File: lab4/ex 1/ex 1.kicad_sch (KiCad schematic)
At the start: 6 parts, among them J1 Conn_01x02_Male, SW1 SW_SPDT

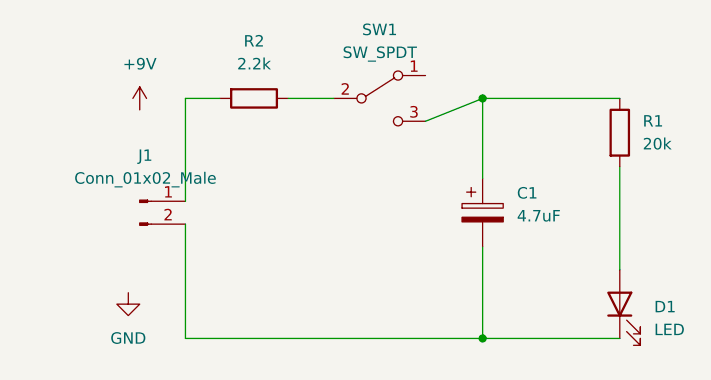
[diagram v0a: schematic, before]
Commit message: Updated schematics to include footprints and created a pcb layout
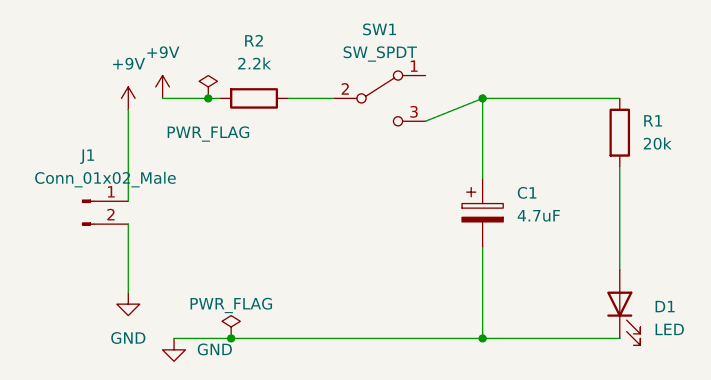
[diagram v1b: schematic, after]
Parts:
- C1: footprint (none) -> Capacitor_THT:C_Radial_D5.0mm_H5.0mm_P2.00mm
- D1: footprint (none) -> LED_THT:LED_D5.0mm
- J1: footprint (none) -> Connector_JST:JST_PH_B2B-PH-K_1x02_P2.00mm_Vertical
- R1, R2: footprint (none) -> Resistor_THT:R_Axial_DIN0516_L15.5mm_D5.0mm_P20.32mm_Horizontal
- SW1: footprint (none) -> Button_Switch_THT:SW_E-Switch_EG1224_SPDT_Angled
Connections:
- net +9V: now also J1.1 (Pin_1), R2.2
- net GND: now also C1.2, D1.1 (K), J1.2 (Pin_2)
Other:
- moved on the sheet: J1
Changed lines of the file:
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@@
 (kicad_sch (version 20211123) (generator eeschema)
   (paper "A4")
+  (junction (at 110.49 69.85) (diameter 0) (color 0 0 0 0)
+  )
   (junction (at 140.97 69.85) (diameter 0) (color 0 0 0 0)
   )
   (junction (at 140.97 96.52) (diameter 0) (color 0 0 0 0)
   )
+  (junction (at 113.03 96.52) (diameter 0) (color 0 0 0 0)
+  )
   (wire (pts (xy 140.97 96.52) (xy 156.21 96.52))
     (stroke (width 0) (type default) (color 0 0 0 0))
@@
     (stroke (width 0) (type default) (color 0 0 0 0))
   )
-  (wire (pts (xy 107.95 96.52) (xy 140.97 96.52))
-    (stroke (width 0) (type default) (color 0 0 0 0))
-  )
-  (wire (pts (xy 107.95 83.82) (xy 107.95 96.52))
-    (stroke (width 0) (type default) (color 0 0 0 0))
-  )
-  (wire (pts (xy 107.95 81.28) (xy 107.95 69.85))
+  (wire (pts (xy 106.68 96.52) (xy 113.03 96.52))
     (stroke (width 0) (type default) (color 0 0 0 0))
   )
@@
     (stroke (width 0) (type default) (color 0 0 0 0))
   )
+  (wire (pts (xy 110.49 69.85) (xy 111.76 69.85))
+    (stroke (width 0) (type default) (color 0 0 0 0))
+  )
+  (wire (pts (xy 101.6 71.12) (xy 101.6 81.28))
+    (stroke (width 0) (type default) (color 0 0 0 0))
+  )
+  (wire (pts (xy 113.03 96.52) (xy 140.97 96.52))
+    (stroke (width 0) (type default) (color 0 0 0 0))
+  )
   (wire (pts (xy 156.21 77.47) (xy 156.21 88.9))
     (stroke (width 0) (type default) (color 0 0 0 0))
   )
+  (wire (pts (xy 101.6 91.44) (xy 101.6 83.82))
+    (stroke (width 0) (type default) (color 0 0 0 0))
+  )
   (wire (pts (xy 140.97 86.36) (xy 140.97 96.52))
     (stroke (width 0) (type default) (color 0 0 0 0))
   )
-  (wire (pts (xy 107.95 69.85) (xy 111.76 69.85))
-    (stroke (width 0) (type default) (color 0 0 0 0))
-  )
-  (symbol (lib_id "power:+9V") (at 102.87 71.12 0) (unit 1)
-    (in_bom yes) (on_board yes)
-    (property "Reference" "#PWR01" (id 0) (at 102.87 74.93 0)
-      (effects (font (size 1.27 1.27)) hide)
-    )
-    (property "Value" "+9V" (id 1) (at 102.87 66.04 0))
-    (property "Footprint" "" (id 2) (at 102.87 71.12 0)
-      (effects (font (size 1.27 1.27)) hide)
-    )
-    (property "Datasheet" "" (id 3) (at 102.87 71.12 0)
+  (wire (pts (xy 105.41 69.85) (xy 110.49 69.85))
+    (stroke (width 0) (type default) (color 0 0 0 0))
+  )
+  (symbol (lib_id "power:+9V") (at 101.6 71.12 0) (unit 1)
+    (in_bom yes) (on_board yes)
+    (property "Reference" "#PWR01" (id 0) (at 101.6 74.93 0)
+      (effects (font (size 1.27 1.27)) hide)
+    )
+    (property "Value" "+9V" (id 1) (at 101.6 66.04 0))
+    (property "Footprint" "" (id 2) (at 101.6 71.12 0)
+      (effects (font (size 1.27 1.27)) hide)
+    )
+    (property "Datasheet" "" (id 3) (at 101.6 71.12 0)
       (effects (font (size 1.27 1.27)) hide)
     )
@@
     (property "Reference" "SW1" (id 0) (at 129.54 62.23 0))
     (property "Value" "SW_SPDT" (id 1) (at 129.54 64.77 0))
-    (property "Footprint" "" (id 2) (at 129.54 69.85 0)
+    (property "Footprint" "Button_Switch_THT:SW_E-Switch_EG1224_SPDT_Angled" (id 2) (at 129.54 69.85 0)
       (effects (font (size 1.27 1.27)) hide)
     )
@@
     (pin "2")
     (pin "3")
+  )
+  (symbol (lib_id "power:PWR_FLAG") (at 113.03 96.52 0) (unit 1)
+    (in_bom yes) (on_board yes)
+    (property "Reference" "#FLG0101" (id 0) (at 113.03 94.615 0)
+      (effects (font (size 1.27 1.27)) hide)
+    )
+    (property "Value" "PWR_FLAG" (id 1) (at 113.03 92.71 0))
+    (property "Footprint" "" (id 2) (at 113.03 96.52 0)
+      (effects (font (size 1.27 1.27)) hide)
+    )
+    (property "Datasheet" "~" (id 3) (at 113.03 96.52 0)
+      (effects (font (size 1.27 1.27)) hide)
+    )
+    (pin "1")
   )
   (symbol (lib_id "Device:LED") (at 156.21 92.71 90) (unit 1)
@@
       (effects (font (size 1.27 1.27)) (justify right))
     )
-    (property "Footprint" "" (id 2) (at 156.21 92.71 0)
+    (property "Footprint" "LED_THT:LED_D5.0mm" (id 2) (at 156.21 92.71 0)
       (effects (font (size 1.27 1.27)) hide)
     )
@@
     (pin "1")
   )
-  (symbol (lib_id "Connector:Conn_01x02_Male") (at 102.87 81.28 0) (unit 1)
-    (in_bom yes) (on_board yes) (fields_autoplaced)
-    (property "Reference" "J1" (id 0) (at 103.505 76.2 0))
-    (property "Value" "Conn_01x02_Male" (id 1) (at 103.505 78.74 0))
-    (property "Footprint" "" (id 2) (at 102.87 81.28 0)
-      (effects (font (size 1.27 1.27)) hide)
-    )
-    (property "Datasheet" "~" (id 3) (at 102.87 81.28 0)
+  (symbol (lib_id "power:+9V") (at 105.41 69.85 0) (unit 1)
+    (in_bom yes) (on_board yes)
+    (property "Reference" "#PWR0101" (id 0) (at 105.41 73.66 0)
+      (effects (font (size 1.27 1.27)) hide)
+    )
+    (property "Value" "+9V" (id 1) (at 105.41 64.77 0))
+    (property "Footprint" "" (id 2) (at 105.41 69.85 0)
+      (effects (font (size 1.27 1.27)) hide)
+    )
+    (property "Datasheet" "" (id 3) (at 105.41 69.85 0)
+      (effects (font (size 1.27 1.27)) hide)
+    )
+    (pin "1")
+  )
+  (symbol (lib_id "Connector:Conn_01x02_Male") (at 96.52 81.28 0) (unit 1)
+    (in_bom yes) (on_board yes)
+    (property "Reference" "J1" (id 0) (at 97.155 76.2 0))
+    (property "Value" "Conn_01x02_Male" (id 1) (at 99.06 78.74 0))
+    (property "Footprint" "Connector_JST:JST_PH_B2B-PH-K_1x02_P2.00mm_Vertical" (id 2) (at 96.52 81.28 0)
+      (effects (font (size 1.27 1.27)) hide)
+    )
+    (property "Datasheet" "~" (id 3) (at 96.52 81.28 0)
       (effects (font (size 1.27 1.27)) hide)
     )
@@
       (effects (font (size 1.27 1.27)) (justify left))
     )
-    (property "Footprint" "" (id 2) (at 141.9352 86.36 0)
+    (property "Footprint" "Capacitor_THT:C_Radial_D5.0mm_H5.0mm_P2.00mm" (id 2) (at 141.9352 86.36 0)
       (effects (font (size 1.27 1.27)) hide)
     )
@@
     (property "Reference" "R2" (id 0) (at 115.57 63.5 90))
     (property "Value" "2.2k" (id 1) (at 115.57 66.04 90))
-    (property "Footprint" "" (id 2) (at 115.57 68.072 90)
+    (property "Footprint" "Resistor_THT:R_Axial_DIN0516_L15.5mm_D5.0mm_P20.32mm_Horizontal" (id 2) (at 115.57 68.072 90)
       (effects (font (size 1.27 1.27)) hide)
     )
@@
     (pin "2")
   )
+  (symbol (lib_id "power:PWR_FLAG") (at 110.49 69.85 0) (unit 1)
+    (in_bom yes) (on_board yes)
+    (property "Reference" "#FLG0102" (id 0) (at 110.49 67.945 0)
+      (effects (font (size 1.27 1.27)) hide)
+    )
+    (property "Value" "PWR_FLAG" (id 1) (at 110.49 73.66 0))
+    (property "Footprint" "" (id 2) (at 110.49 69.85 0)
+      (effects (font (size 1.27 1.27)) hide)
+    )
+    (property "Datasheet" "~" (id 3) (at 110.49 69.85 0)
+      (effects (font (size 1.27 1.27)) hide)
+    )
+    (pin "1")
+  )
+  (symbol (lib_id "power:GND") (at 106.68 96.52 0) (unit 1)
+    (in_bom yes) (on_board yes) (fields_autoplaced)
+    (property "Reference" "#PWR0102" (id 0) (at 106.68 102.87 0)
+      (effects (font (size 1.27 1.27)) hide)
+    )
+    (property "Value" "GND" (id 1) (at 109.22 97.7899 0)
+      (effects (font (size 1.27 1.27)) (justify left))
+    )
+    (property "Footprint" "" (id 2) (at 106.68 96.52 0)
+      (effects (font (size 1.27 1.27)) hide)
+    )
+    (property "Datasheet" "" (id 3) (at 106.68 96.52 0)
+      (effects (font (size 1.27 1.27)) hide)
+    )
+    (pin "1")
+  )
   (symbol (lib_id "Device:R") (at 156.21 73.66 0) (unit 1)
     (in_bom yes) (on_board yes) (fields_autoplaced)
@@
       (effects (font (size 1.27 1.27)) (justify left))
     )
-    (property "Footprint" "" (id 2) (at 154.432 73.66 90)
+    (property "Footprint" "Resistor_THT:R_Axial_DIN0516_L15.5mm_D5.0mm_P20.32mm_Horizontal" (id 2) (at 154.432 73.66 90)
       (effects (font (size 1.27 1.27)) hide)
     )
@@
   )
   (symbol_instances
+    (path "/2d91e471-708e-42eb-883b-1bac5721cbcd"
+      (reference "#FLG0101") (unit 1) (value "PWR_FLAG") (footprint "")
+    )
+    (path "/c8428026-bf09-48ca-8084-a667ff80b987"
+      (reference "#FLG0102") (unit 1) (value "PWR_FLAG") (footprint "")
+    )
     (path "/06ac46e9-c18d-4884-aa55-c7c1cbcc004b"
       (reference "#PWR01") (unit 1) (value "+9V") (footprint "")
@@
       (reference "#PWR02") (unit 1) (value "GND") (footprint "")
     )
+    (path "/7b0484b7-9941-45db-ac2f-e5ea7340386b"
+      (reference "#PWR0101") (unit 1) (value "+9V") (footprint "")
+    )
+    (path "/e8a387bc-7126-4786-8248-6c4ba9a8f413"
+      (reference "#PWR0102") (unit 1) (value "GND") (footprint "")
+    )
     (path "/99f1b54f-9360-4f32-81ea-718aa984aa84"
-      (reference "C1") (unit 1) (value "4.7uF") (footprint "")
+      (reference "C1") (unit 1) (value "4.7uF") (footprint "Capacitor_THT:C_Radial_D5.0mm_H5.0mm_P2.00mm")
     )
     (path "/309ebb44-a2f3-4eb1-bd0f-0f88f32a8f2d"
-      (reference "D1") (unit 1) (value "LED") (footprint "")
+      (reference "D1") (unit 1) (value "LED") (footprint "LED_THT:LED_D5.0mm")
     )
     (path "/8769ea8b-c8aa-437d-a5f8-8c400cb61946"
-      (reference "J1") (unit 1) (value "Conn_01x02_Male") (footprint "")
+      (reference "J1") (unit 1) (value "Conn_01x02_Male") (footprint "Connector_JST:JST_PH_B2B-PH-K_1x02_P2.00mm_Vertical")
     )
     (path "/f9920d9b-c0a2-488c-8f60-830cb532d3d6"
-      (reference "R1") (unit 1) (value "20k") (footprint "")
+      (reference "R1") (unit 1) (value "20k") (footprint "Resistor_THT:R_Axial_DIN0516_L15.5mm_D5.0mm_P20.32mm_Horizontal")
     )
     (path "/b45a8b59-e066-44dd-b29f-d6af8479140c"
-      (reference "R2") (unit 1) (value "2.2k") (footprint "")
+      (reference "R2") (unit 1) (value "2.2k") (footprint "Resistor_THT:R_Axial_DIN0516_L15.5mm_D5.0mm_P20.32mm_Horizontal")
     )
     (path "/07b54438-4c7d-4e6d-9f9f-7656b0dd0948"
-      (reference "SW1") (unit 1) (value "SW_SPDT") (footprint "")
-    )
-  )
+      (reference "SW1") (unit 1) (value "SW_SPDT") (footprint "Button_Switch_THT:SW_E-Switch_EG1224_SPDT_Angled")
+    )
+  )
